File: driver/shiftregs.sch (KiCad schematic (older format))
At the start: 32 parts, among them IC1101 74HC595, IC1102 74HC595, IC1103 74HC595, IC1104 74HC595, IC1105 74HC595, IC1106 74HC595, IC1107 74HC595, IC1108 74HC595, IC1109 74HC595, IC1110 74HC595, IC1111 74HC595, IC1112 74HC595, IC1113 74HC595, IC1114 74HC595, IC1115 74HC595, IC1116 74HC595

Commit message: Finish sch, start PCB
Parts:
- C1101, C1102, C1103, C1104, C1105, C1106, C1107, C1108, C1109, C1110, C1111, C1112, C1113, C1114, C1115, C1116: Farnell (none) -> 2320803; Voltage (none) -> 50V
- IC1101, IC1106, IC1111, IC1116: Farnell 2425499 -> 1607848
- IC1102: renamed from IC1105; Farnell 2425499 -> 1607848
- IC1103: renamed from IC1109; Farnell 2425499 -> 1607848
- IC1104: renamed from IC1113; Farnell 2425499 -> 1607848
- IC1105: renamed from IC1102; Farnell 2425499 -> 1607848
- IC1107: renamed from IC1110; Farnell 2425499 -> 1607848
- IC1108: renamed from IC1114; Farnell 2425499 -> 1607848
- IC1109: renamed from IC1103; Farnell 2425499 -> 1607848
- IC1110: renamed from IC1107; Farnell 2425499 -> 1607848
- IC1112: renamed from IC1115; Farnell 2425499 -> 1607848
- IC1113: renamed from IC1104; Farnell 2425499 -> 1607848
- IC1114: renamed from IC1108; Farnell 2425499 -> 1607848
- IC1115: renamed from IC1112; Farnell 2425499 -> 1607848

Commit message: WIP PCB
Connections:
- net DSAO: now reaches IC1108.9 (Q7S)
- net DSKO: now reaches IC1116.9 (Q7S)
- no-connect marks 2 -> 0
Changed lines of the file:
@@
 Text Label 9250 3050 0    50   ~ 0
 GA64
-NoConn ~ 9200 3150
 Text Label 3100 3950 0    50   ~ 0
 GK1
@@
 Text Label 9250 6050 0    50   ~ 0
 GK64
-NoConn ~ 9200 6150
 Text Label 7200 5350 0    50   ~ 0
 GK49
@@
 Wire Wire Line
 	8300 6150 7150 6150
+Text HLabel 9600 3150 2    50   Output ~ 0
+DSAO
+Wire Wire Line
+	9600 3150 9200 3150
+Text HLabel 9600 6150 2    50   Output ~ 0
+DSKO
+Wire Wire Line
+	9600 6150 9200 6150
 Wire Bus Line
 	9550 2200 9550 2950

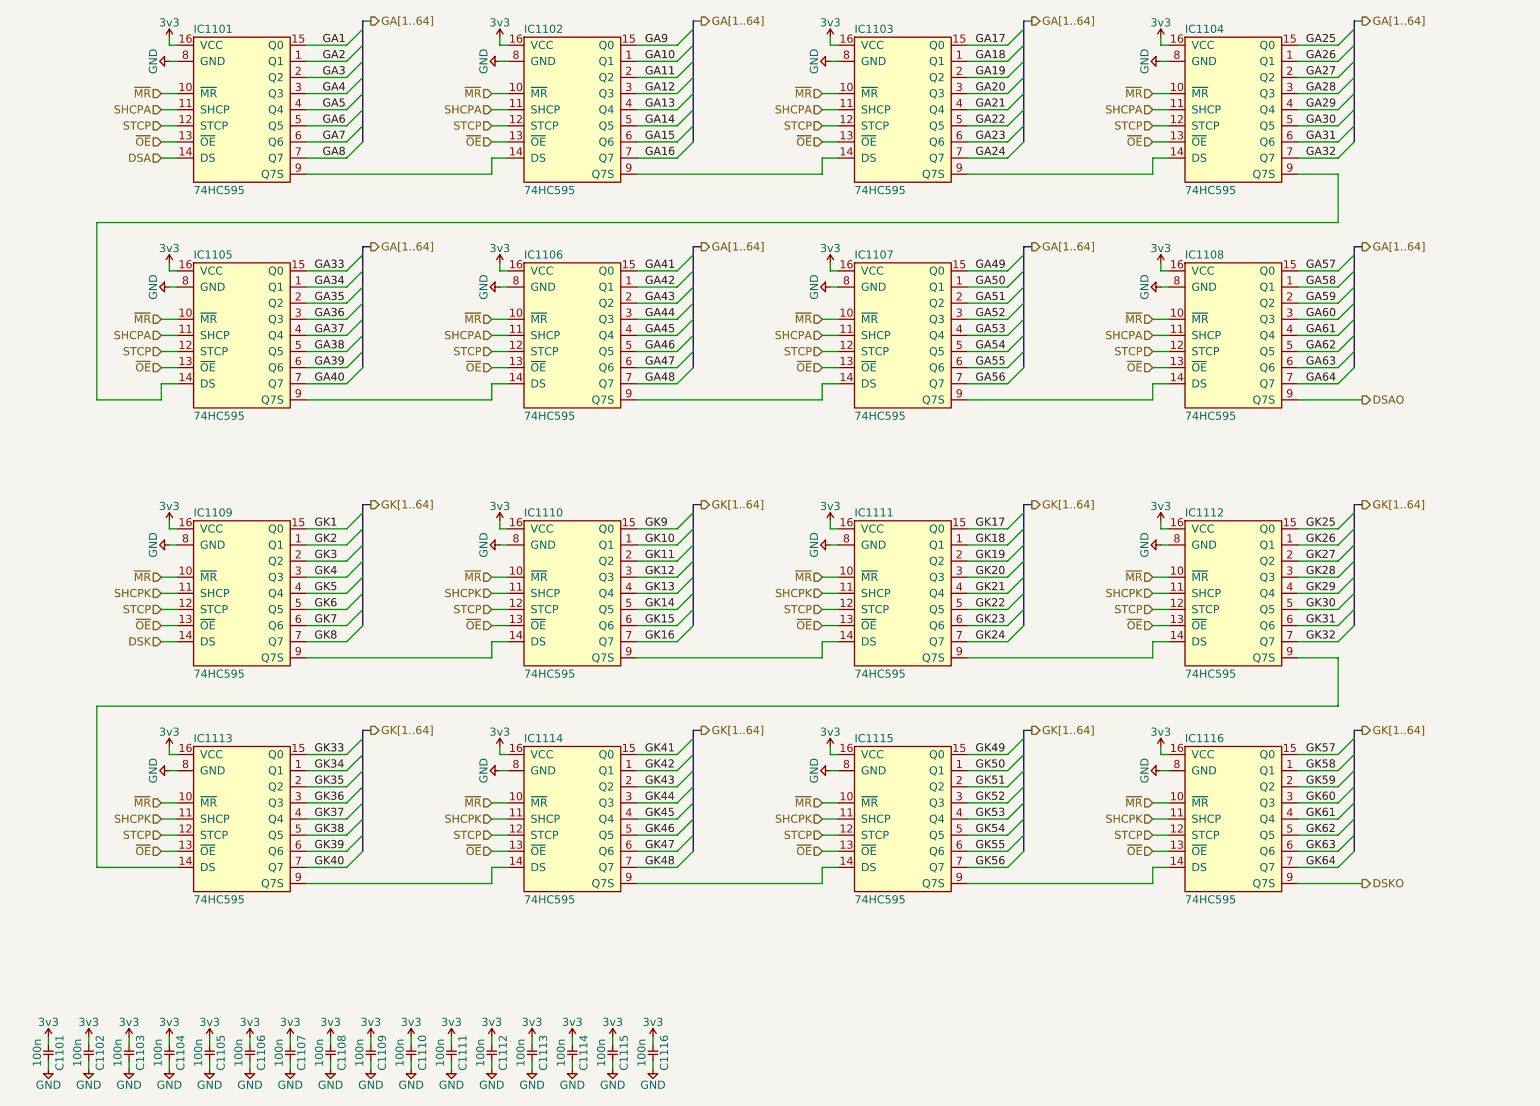
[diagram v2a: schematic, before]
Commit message: Start work on 32ch board
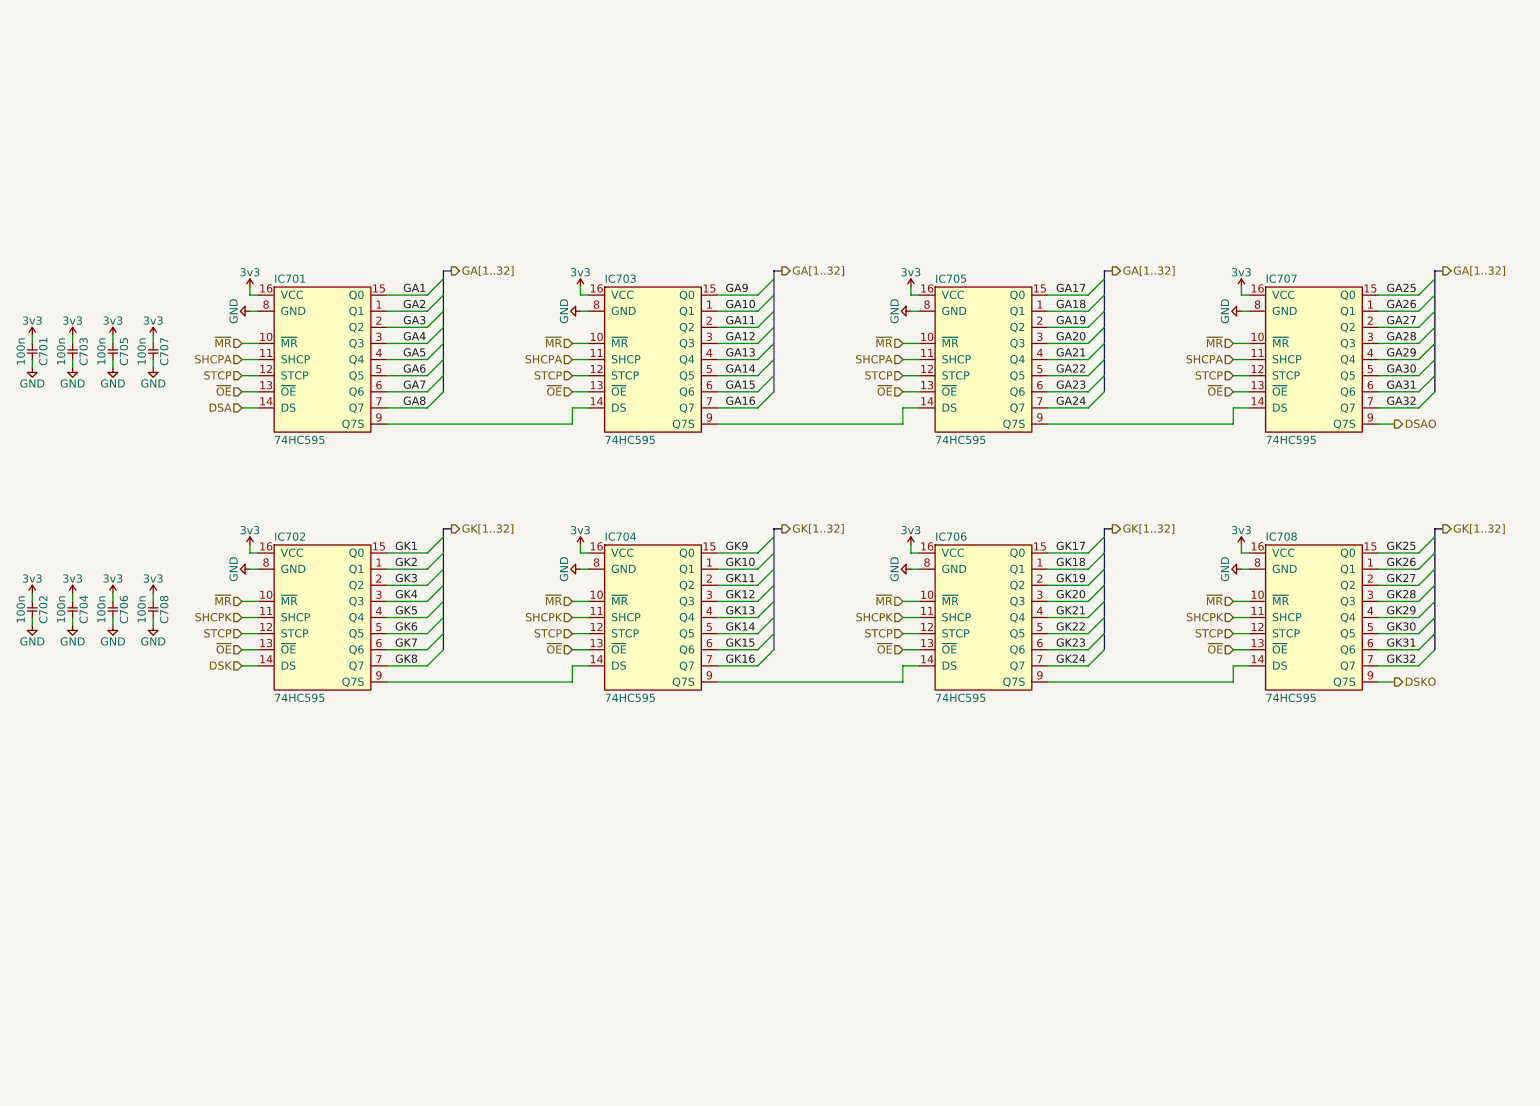
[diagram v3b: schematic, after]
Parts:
- removed C1109, C1110, C1111, C1112, C1113, C1114, C1115, C1116: 100n, agg:0603, symbol agg-kicad:C
- removed IC1105, IC1106, IC1107, IC1108, IC1113, IC1114, IC1115, IC1116: 74HC595, agg:TSSOP-16, symbol agg-kicad:74HC595
- renumbered C1101 to C701, C1105 to C702, C1102 to C703, C1106 to C704, C1103 to C705, C1107 to C706, C1104 to C707, C1108 to C708, IC1101 to IC701, IC1109 to IC702, IC1102 to IC703, IC1110 to IC704, IC1103 to IC705, IC1111 to IC706, IC1104 to IC707, IC1112 to IC708
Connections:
- net DSAO: now also IC707.9 (Q7S)
- net DSKO: now also IC708.9 (Q7S)
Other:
- moved on the sheet: C701, C702, C703, C704, C705, C706, C707, C708, IC701, IC702, IC703, IC704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

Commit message: more layout work
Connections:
- net GA1: now also IC701.7 (Q7); no longer IC701.15 (Q0)
- net GA10: now also IC703.6 (Q6); no longer IC703.1 (Q1)
- net GA11: now also IC703.5 (Q5); no longer IC703.2 (Q2)
- net GA12: now also IC703.4 (Q4); no longer IC703.3 (Q3)
- net GA13: now also IC703.3 (Q3); no longer IC703.4 (Q4)
- net GA14: now also IC703.2 (Q2); no longer IC703.5 (Q5)
- net GA15: now also IC703.1 (Q1); no longer IC703.6 (Q6)
- net GA16: now also IC703.15 (Q0); no longer IC703.7 (Q7)
- net GA17: now also IC705.7 (Q7); no longer IC705.15 (Q0)
- net GA18: now also IC705.6 (Q6); no longer IC705.1 (Q1)
- net GA19: now also IC705.5 (Q5); no longer IC705.2 (Q2)
- net GA2: now also IC701.6 (Q6); no longer IC701.1 (Q1)
- net GA20: now also IC705.4 (Q4); no longer IC705.3 (Q3)
- net GA21: now also IC705.3 (Q3); no longer IC705.4 (Q4)
- net GA22: now also IC705.2 (Q2); no longer IC705.5 (Q5)
- net GA23: now also IC705.1 (Q1); no longer IC705.6 (Q6)
- net GA24: now also IC705.15 (Q0); no longer IC705.7 (Q7)
- net GA25: now also IC707.7 (Q7); no longer IC707.15 (Q0)
- net GA26: now also IC707.6 (Q6); no longer IC707.1 (Q1)
- net GA27: now also IC707.5 (Q5); no longer IC707.2 (Q2)
- net GA28: now also IC707.4 (Q4); no longer IC707.3 (Q3)
- net GA29: now also IC707.3 (Q3); no longer IC707.4 (Q4)
- net GA3: now also IC701.5 (Q5); no longer IC701.2 (Q2)
- net GA30: now also IC707.2 (Q2); no longer IC707.5 (Q5)
- net GA31: now also IC707.1 (Q1); no longer IC707.6 (Q6)
- net GA32: now also IC707.15 (Q0); no longer IC707.7 (Q7)
- net GA4: now also IC701.4 (Q4); no longer IC701.3 (Q3)
- net GA5: now also IC701.3 (Q3); no longer IC701.4 (Q4)
- net GA6: now also IC701.2 (Q2); no longer IC701.5 (Q5)
- net GA7: now also IC701.1 (Q1); no longer IC701.6 (Q6)
- net GA8: now also IC701.15 (Q0); no longer IC701.7 (Q7)
- net GA9: now also IC703.7 (Q7); no longer IC703.15 (Q0)
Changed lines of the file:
@@
 Wire Wire Line
 	8800 4800 8900 4800
+Text Label 3650 3200 0    50   ~ 0
+GA1
+Text Label 3650 3100 0    50   ~ 0
+GA2
+Text Label 3650 3000 0    50   ~ 0
+GA3
+Text Label 3650 2900 0    50   ~ 0
+GA4
+Text Label 3650 2800 0    50   ~ 0
+GA5
+Text Label 3650 2700 0    50   ~ 0
+GA6
+Text Label 3650 2600 0    50   ~ 0
+GA7
 Text Label 3650 2500 0    50   ~ 0
-GA1
-Text Label 3650 2600 0    50   ~ 0
-GA2
-Text Label 3650 2700 0    50   ~ 0
-GA3
-Text Label 3650 2800 0    50   ~ 0
-GA4
-Text Label 3650 2900 0    50   ~ 0
-GA5
-Text Label 3650 3000 0    50   ~ 0
-GA6
-Text Label 3650 3100 0    50   ~ 0
-GA7
-Text Label 3650 3200 0    50   ~ 0
 GA8
+Text Label 5650 3200 0    50   ~ 0
+GA9
+Text Label 5650 3100 0    50   ~ 0
+GA10
+Text Label 5650 3000 0    50   ~ 0
+GA11
+Text Label 5650 2900 0    50   ~ 0
+GA12
+Text Label 5650 2800 0    50   ~ 0
+GA13
+Text Label 5650 2700 0    50   ~ 0
+GA14
+Text Label 5650 2600 0    50   ~ 0
+GA15
 Text Label 5650 2500 0    50   ~ 0
-GA9
-Text Label 5650 2600 0    50   ~ 0
-GA10
-Text Label 5650 2700 0    50   ~ 0
-GA11
-Text Label 5650 2800 0    50   ~ 0
-GA12
-Text Label 5650 2900 0    50   ~ 0
-GA13
-Text Label 5650 3000 0    50   ~ 0
-GA14
-Text Label 5650 3100 0    50   ~ 0
-GA15
-Text Label 5650 3200 0    50   ~ 0
 GA16
+Text Label 7700 3200 0    50   ~ 0
+GA17
+Text Label 7700 3100 0    50   ~ 0
+GA18
+Text Label 7700 3000 0    50   ~ 0
+GA19
+Text Label 7700 2900 0    50   ~ 0
+GA20
+Text Label 7700 2800 0    50   ~ 0
+GA21
+Text Label 7700 2700 0    50   ~ 0
+GA22
+Text Label 7700 2600 0    50   ~ 0
+GA23
 Text Label 7700 2500 0    50   ~ 0
-GA17
-Text Label 7700 2600 0    50   ~ 0
-GA18
-Text Label 7700 2700 0    50   ~ 0
-GA19
-Text Label 7700 2800 0    50   ~ 0
-GA20
-Text Label 7700 2900 0    50   ~ 0
-GA21
-Text Label 7700 3000 0    50   ~ 0
-GA22
-Text Label 7700 3100 0    50   ~ 0
-GA23
-Text Label 7700 3200 0    50   ~ 0
 GA24
+Text Label 9750 3200 0    50   ~ 0
+GA25
+Text Label 9750 3100 0    50   ~ 0
+GA26
+Text Label 9750 3000 0    50   ~ 0
+GA27
+Text Label 9750 2900 0    50   ~ 0
+GA28
+Text Label 9750 2800 0    50   ~ 0
+GA29
+Text Label 9750 2700 0    50   ~ 0
+GA30
+Text Label 9750 2600 0    50   ~ 0
+GA31
 Text Label 9750 2500 0    50   ~ 0
-GA25
-Text Label 9750 2600 0    50   ~ 0
-GA26
-Text Label 9750 2700 0    50   ~ 0
-GA27
-Text Label 9750 2800 0    50   ~ 0
-GA28
-Text Label 9750 2900 0    50   ~ 0
-GA29
-Text Label 9750 3000 0    50   ~ 0
-GA30
-Text Label 9750 3100 0    50   ~ 0
-GA31
-Text Label 9750 3200 0    50   ~ 0
 GA32
 Text Label 3600 4100 0    50   ~ 0
